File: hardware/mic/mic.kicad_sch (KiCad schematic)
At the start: 14 parts, among them U1 TL072, U2 CR2013-MI2120, U3 ESP32-C3-DevKitM-1

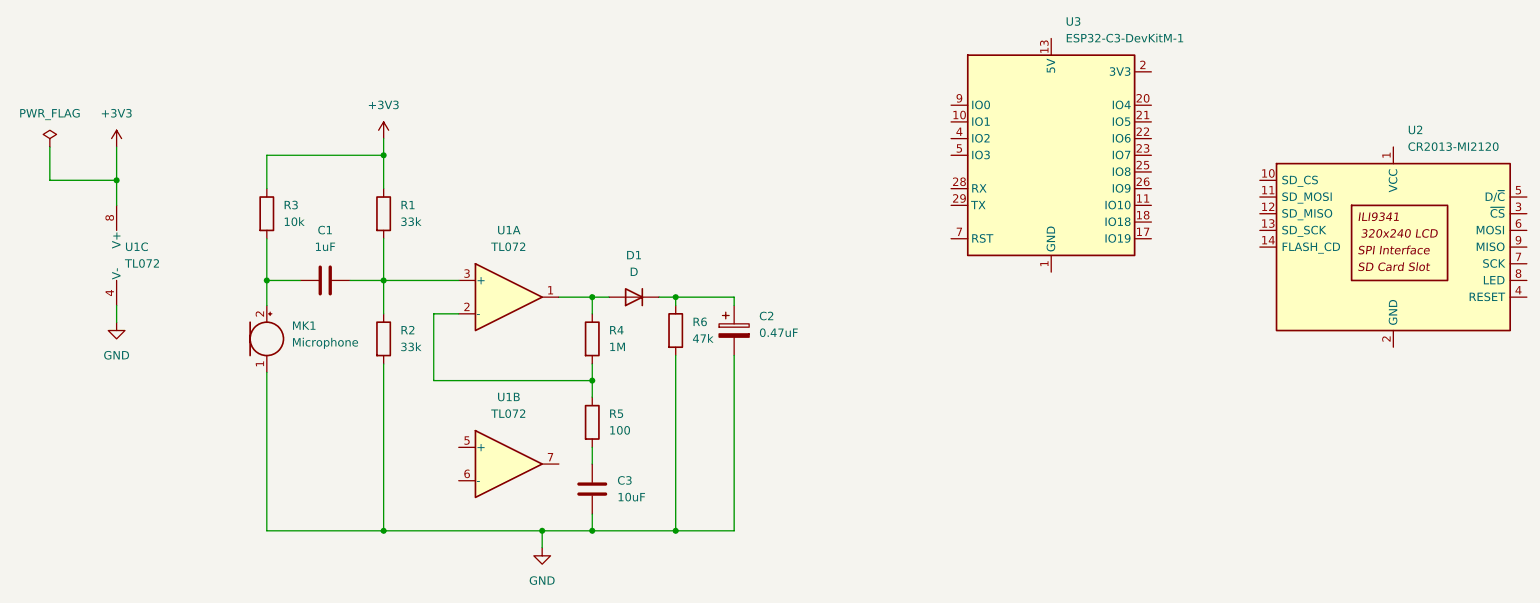
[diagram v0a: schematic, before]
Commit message: add mic amplifier circuit
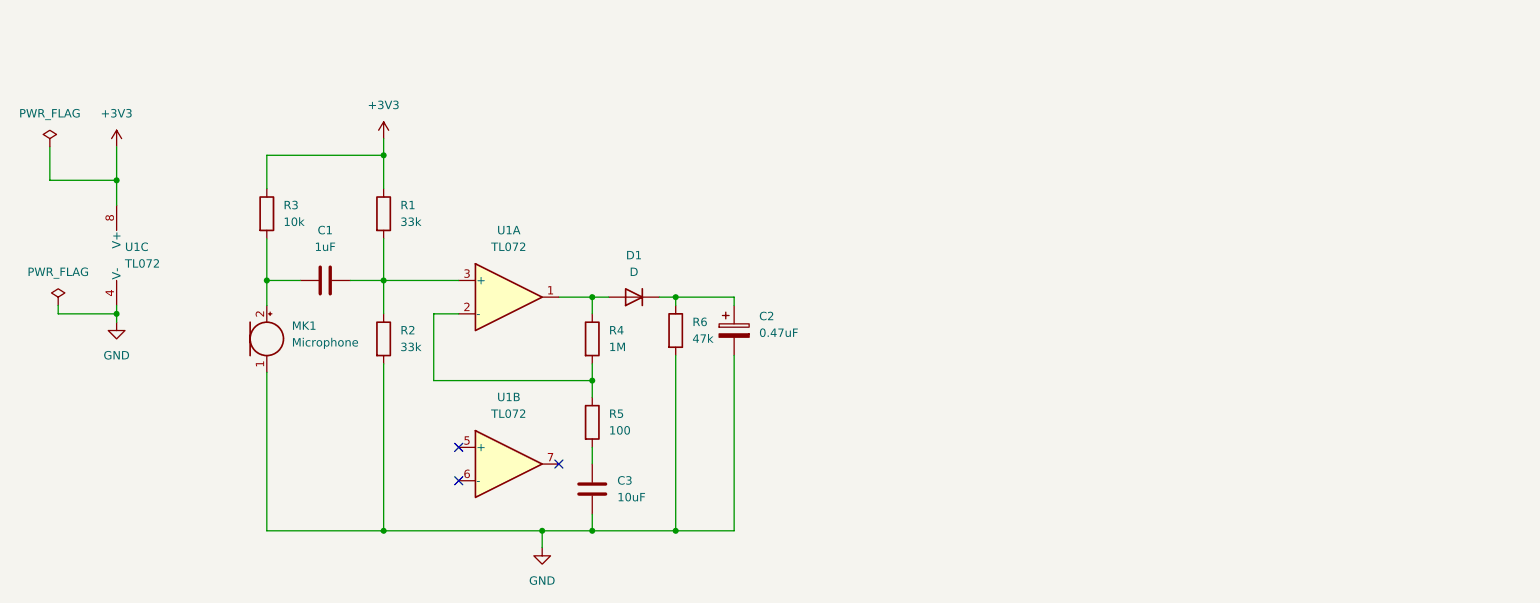
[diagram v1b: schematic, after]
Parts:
- removed U2: CR2013-MI2120, Display:CR2013-MI2120, symbol Driver_Display:CR2013-MI2120
- removed U3: ESP32-C3-DevKitM-1, RF_Module:ESP32-C3-DevKitM-1, symbol RF_Module:ESP32-C3-DevKitM-1
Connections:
- no-connect marks 0 -> 3
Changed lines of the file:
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@@
+	)
+	(junction
+		(at 41.91 87.63)
+		(diameter 0)
+		(color 0 0 0 0)
 	)
 	(junction
@@
 		(color 0 0 0 0)
 	)
+	(no_connect
+		(at 109.22 110.49)
+	)
+	(no_connect
+		(at 93.98 113.03)
+	)
+	(no_connect
+		(at 93.98 107.95)
+	)
 	(wire
 		(pts
@@
 	(wire
 		(pts
-			(xy 41.91 88.9) (xy 41.91 86.36)
+			(xy 41.91 88.9) (xy 41.91 87.63)
 		)
 		(stroke
@@
 	(wire
 		(pts
+			(xy 33.02 86.36) (xy 33.02 87.63)
+		)
+		(stroke
+			(width 0)
+			(type default)
+		)
+	)
+	(wire
+		(pts
 			(xy 64.77 96.52) (xy 64.77 120.65)
 		)
@@
 	(wire
 		(pts
+			(xy 41.91 87.63) (xy 41.91 86.36)
+		)
+		(stroke
+			(width 0)
+			(type default)
+		)
+	)
+	(wire
+		(pts
 			(xy 82.55 60.96) (xy 82.55 63.5)
 		)
@@
 		(pts
 			(xy 127 85.09) (xy 124.46 85.09)
+		)
+		(stroke
+			(width 0)
+			(type default)
+		)
+	)
+	(wire
+		(pts
+			(xy 33.02 87.63) (xy 41.91 87.63)
 		)
 		(stroke
@@
 	)
 	(symbol
-		(lib_id "Driver_Display:CR2013-MI2120")
-		(at 236.22 77.47 0)
-		(unit 1)
-		(exclude_from_sim no)
-		(in_bom yes)
-		(on_board yes)
-		(dnp no)
-		(fields_autoplaced yes)
-		(property "Reference" "U2"
-			(at 238.4141 59.69 0)
-			(effects
-				(font
-					(size 1.27 1.27)
-				)
-				(justify left)
-			)
-		)
-		(property "Value" "CR2013-MI2120"
-			(at 238.4141 62.23 0)
-			(effects
-				(font
-					(size 1.27 1.27)
-				)
-				(justify left)
-			)
-		)
-		(property "Footprint" "Display:CR2013-MI2120"
-			(at 236.22 95.25 0)
-			(effects
-				(font
-					(size 1.27 1.27)
-				)
-				(hide yes)
-			)
-		)
-		(property "Datasheet" "http://pan.baidu.com/s/11Y990"
-			(at 219.71 64.77 0)
-			(effects
-				(font
-					(size 1.27 1.27)
-				)
-				(hide yes)
-			)
-		)
-		(property "Description" "ILI9341 controller, SPI TFT LCD Display, 9-pin breakout PCB, 4-pin SD card interface, 5V/3.3V"
-			(at 236.22 77.47 0)
-			(effects
-				(font
-					(size 1.27 1.27)
-				)
-				(hide yes)
-			)
-		)
-		(pin "2"
-		)
-		(pin "7"
-		)
-		(pin "6"
-		)
-		(pin "10"
-		)
-		(pin "13"
-		)
-		(pin "12"
-		)
-		(pin "1"
-		)
-		(pin "11"
-		)
-		(pin "14"
-		)
-		(pin "8"
-		)
-		(pin "3"
-		)
-		(pin "5"
-		)
-		(pin "9"
-		)
-		(pin "4"
-		)
-		(instances
-			(project ""
-				(path "/b6a30cd2-60c1-4ed7-9717-182f03282519"
-					(reference "U2")
-					(unit 1)
-				)
-			)
-		)
-	)
-	(symbol
 		(lib_id "power:GND")
 		(at 41.91 88.9 0)
@@
 	(symbol
 		(lib_id "power:PWR_FLAG")
+		(at 33.02 86.36 0)
+		(unit 1)
+		(exclude_from_sim no)
+		(in_bom yes)
+		(on_board yes)
+		(dnp no)
+		(fields_autoplaced yes)
+		(property "Reference" "#FLG02"
+			(at 33.02 84.455 0)
+			(effects
+				(font
+					(size 1.27 1.27)
+				)
+				(hide yes)
+			)
+		)
+		(property "Value" "PWR_FLAG"
+			(at 33.02 81.28 0)
+			(effects
+				(font
+					(size 1.27 1.27)
+				)
+			)
+		)
+		(property "Footprint" ""
+			(at 33.02 86.36 0)
+			(effects
+				(font
+					(size 1.27 1.27)
+				)
+				(hide yes)
+			)
+		)
+		(property "Datasheet" "~"
+			(at 33.02 86.36 0)
+			(effects
+				(font
+					(size 1.27 1.27)
+				)
+				(hide yes)
+			)
+		)
+		(property "Description" "Special symbol for telling ERC where power comes from"
+			(at 33.02 86.36 0)
+			(effects
+				(font
+					(size 1.27 1.27)
+				)
+				(hide yes)
+			)
+		)
+		(pin "1"
+		)
+		(instances
+			(project "mic"
+				(path "/b6a30cd2-60c1-4ed7-9717-182f03282519"
+					(reference "#FLG02")
+					(unit 1)
+				)
+			)
+		)
+	)
+	(symbol
+		(lib_id "power:PWR_FLAG")
 		(at 31.75 62.23 0)
 		(unit 1)
@@
 					(unit 1)
 				)
-			)
-		)
-	)
-	(symbol
-		(lib_id "RF_Module:ESP32-C3-DevKitM-1")
-		(at 184.15 63.5 0)
-		(unit 1)
-		(exclude_from_sim no)
-		(in_bom yes)
-		(on_board yes)
-		(dnp no)
-		(fields_autoplaced yes)
-		(property "Reference" "U3"
-			(at 186.3441 43.18 0)
-			(effects
-				(font
-					(size 1.27 1.27)
-				)
-				(justify left)
-			)
-		)
-		(property "Value" "ESP32-C3-DevKitM-1"
-			(at 186.3441 45.72 0)
-			(effects
-				(font
-					(size 1.27 1.27)
-				)
-				(justify left)
-			)
-		)
-		(property "Footprint" "RF_Module:ESP32-C3-DevKitM-1"
-			(at 184.15 88.9 0)
-			(effects
-				(font
-					(size 1.27 1.27)
-				)
-				(hide yes)
-			)
-		)
-		(property "Datasheet" "https://docs.espressif.com/projects/esp-idf/en/latest/esp32c3/hw-reference/esp32c3/user-guide-devkitm-1.html"
-			(at 184.15 93.98 0)
-			(effects
-				(font
-					(size 1.27 1.27)
-				)
-				(hide yes)
-			)
-		)
-		(property "Description" "Development board featuring ESP32-C3-MINI-1 module"
-			(at 184.15 91.44 0)
-			(effects
-				(font
-					(size 1.27 1.27)
-				)
-				(hide yes)
-			)
-		)
-		(pin "3"
-		)
-		(pin "23"
-		)
-		(pin "27"
-		)
-		(pin "29"
-		)
-		(pin "19"
-		)
-		(pin "26"
-		)
-		(pin "9"
-		)
-		(pin "12"
-		)
-		(pin "20"
-		)
-		(pin "13"
-		)
-		(pin "15"
-		)
-		(pin "30"
-		)
-		(pin "6"
-		)
-		(pin "14"
-		)
-		(pin "28"
-		)
-		(pin "10"
-		)
-		(pin "1"
-		)
-		(pin "2"
-		)
-		(pin "11"
-		)
-		(pin "25"
-		)
-		(pin "22"
-		)
-		(pin "24"
-		)
-		(pin "5"
-		)
-		(pin "16"
-		)
-		(pin "17"
-		)
-		(pin "18"
-		)
-		(pin "8"
-		)
-		(pin "21"
-		)
-		(pin "4"
-		)
-		(pin "7"
-		)
-		(instances
-			(project ""
-				(path "/b6a30cd2-60c1-4ed7-9717-182f03282519"
-					(reference "U3")
-					(unit 1)
-				)
